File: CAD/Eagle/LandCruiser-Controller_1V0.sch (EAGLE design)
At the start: 37 parts, among them U101 MEGA8-P, U221 SN75240, U301 MIC2981/2982, U511 LM7805, X201 WEIDMUELLER 1234600000, X321 WEIDMUELLER 1234600000, X401 I2C

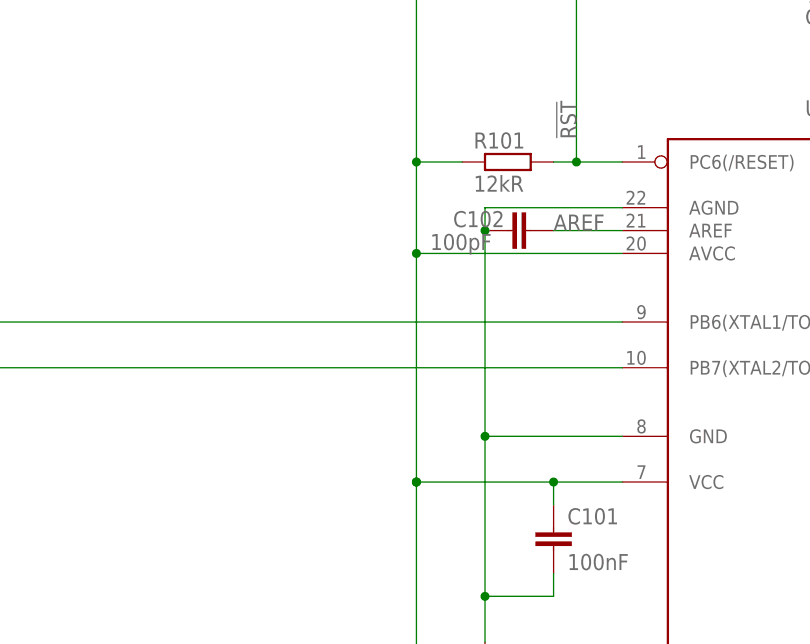
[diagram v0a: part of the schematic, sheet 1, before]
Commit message: HW_V1.0 - MPU - AVCC with 10uH for better ADC results
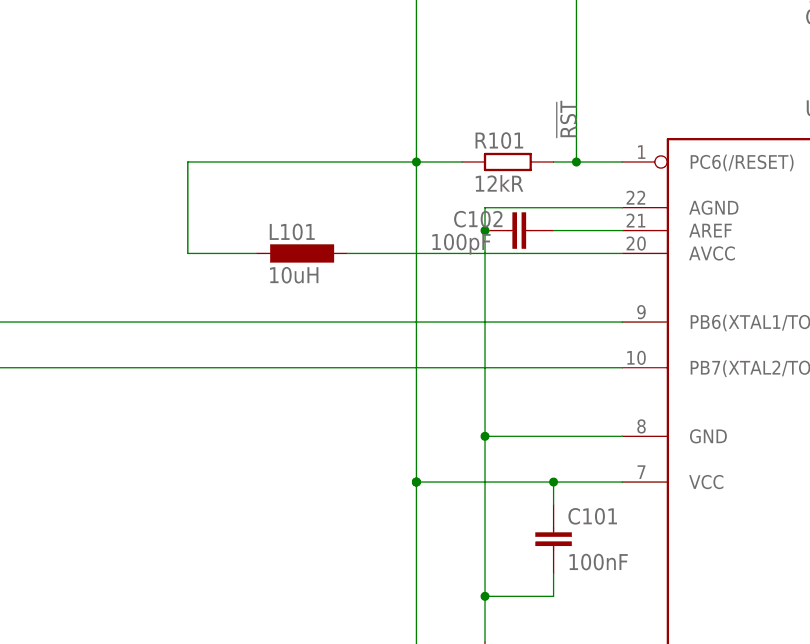
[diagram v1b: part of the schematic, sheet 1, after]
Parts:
- added L101: 10uH, rcl:L-EUL1812
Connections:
- net AREF renamed MP_AREF
- new net MP_AVCC: L101.1, U101.AVCC
- net +5V: now also L101.2; no longer U101.AVCC
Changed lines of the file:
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@@
 <part name="P+12V_1" library="df4iah_supply" deviceset="+12V" device=""/>
 <part name="FRAME7" library="df4iah_frame" deviceset="A4L-LOC" device="" value="I2C connector"/>
+<part name="L101" library="rcl" deviceset="L-EU" device="L1812" value="10uH"/>
 </parts>
 <sheets>
@@
 <instance part="X111" gate="G$1" x="124.46" y="152.4"/>
 <instance part="GND111" gate="1" x="134.62" y="137.16"/>
+<instance part="L101" gate="G$1" x="76.2" y="109.22" rot="R270"/>
 </instances>
 <busses>
@@
 </segment>
 </net>
-<net name="AREF" class="0">
+<net name="MP_AREF" class="0">
 <segment>
 <pinref part="C102" gate="G$1" pin="2"/>
 <wire x1="104.14" y1="111.76" x2="111.76" y2="111.76" width="0.1524" layer="91"/>
 <pinref part="U101" gate="G$1" pin="AREF"/>
-<label x="104.14" y="111.76" size="1.778" layer="95"/>
 </segment>
 </net>
@@
 <wire x1="88.9" y1="167.64" x2="88.9" y2="162.56" width="0.1524" layer="91"/>
 <wire x1="88.9" y1="162.56" x2="88.9" y2="119.38" width="0.1524" layer="91"/>
-<wire x1="88.9" y1="119.38" x2="88.9" y2="109.22" width="0.1524" layer="91"/>
-<wire x1="88.9" y1="109.22" x2="88.9" y2="83.82" width="0.1524" layer="91"/>
+<wire x1="88.9" y1="119.38" x2="88.9" y2="83.82" width="0.1524" layer="91"/>
 <junction x="88.9" y="83.82"/>
 <wire x1="88.9" y1="119.38" x2="93.98" y2="119.38" width="0.1524" layer="91"/>
 <junction x="88.9" y="119.38"/>
 <pinref part="R101" gate="G$1" pin="1"/>
-<pinref part="U101" gate="G$1" pin="AVCC"/>
-<wire x1="111.76" y1="109.22" x2="88.9" y2="109.22" width="0.1524" layer="91"/>
-<junction x="88.9" y="109.22"/>
 <pinref part="U101" gate="G$1" pin="VCC@1"/>
 <wire x1="88.9" y1="83.82" x2="104.14" y2="83.82" width="0.1524" layer="91"/>
@@
 <wire x1="104.14" y1="83.82" x2="104.14" y2="81.28" width="0.1524" layer="91"/>
 <junction x="104.14" y="83.82"/>
-</segment>
-</net>
+<wire x1="88.9" y1="119.38" x2="63.5" y2="119.38" width="0.1524" layer="91"/>
+<wire x1="63.5" y1="119.38" x2="63.5" y2="109.22" width="0.1524" layer="91"/>
+<pinref part="L101" gate="G$1" pin="2"/>
+<wire x1="63.5" y1="109.22" x2="71.12" y2="109.22" width="0.1524" layer="91"/>
+</segment>
+</net>
+<net name="MP_AVCC" class="0">
+<segment>
+<pinref part="U101" gate="G$1" pin="AVCC"/>
+<pinref part="L101" gate="G$1" pin="1"/>
+<wire x1="111.76" y1="109.22" x2="81.28" y2="109.22" width="0.1524" layer="91"/>
+</segment>
+</net>

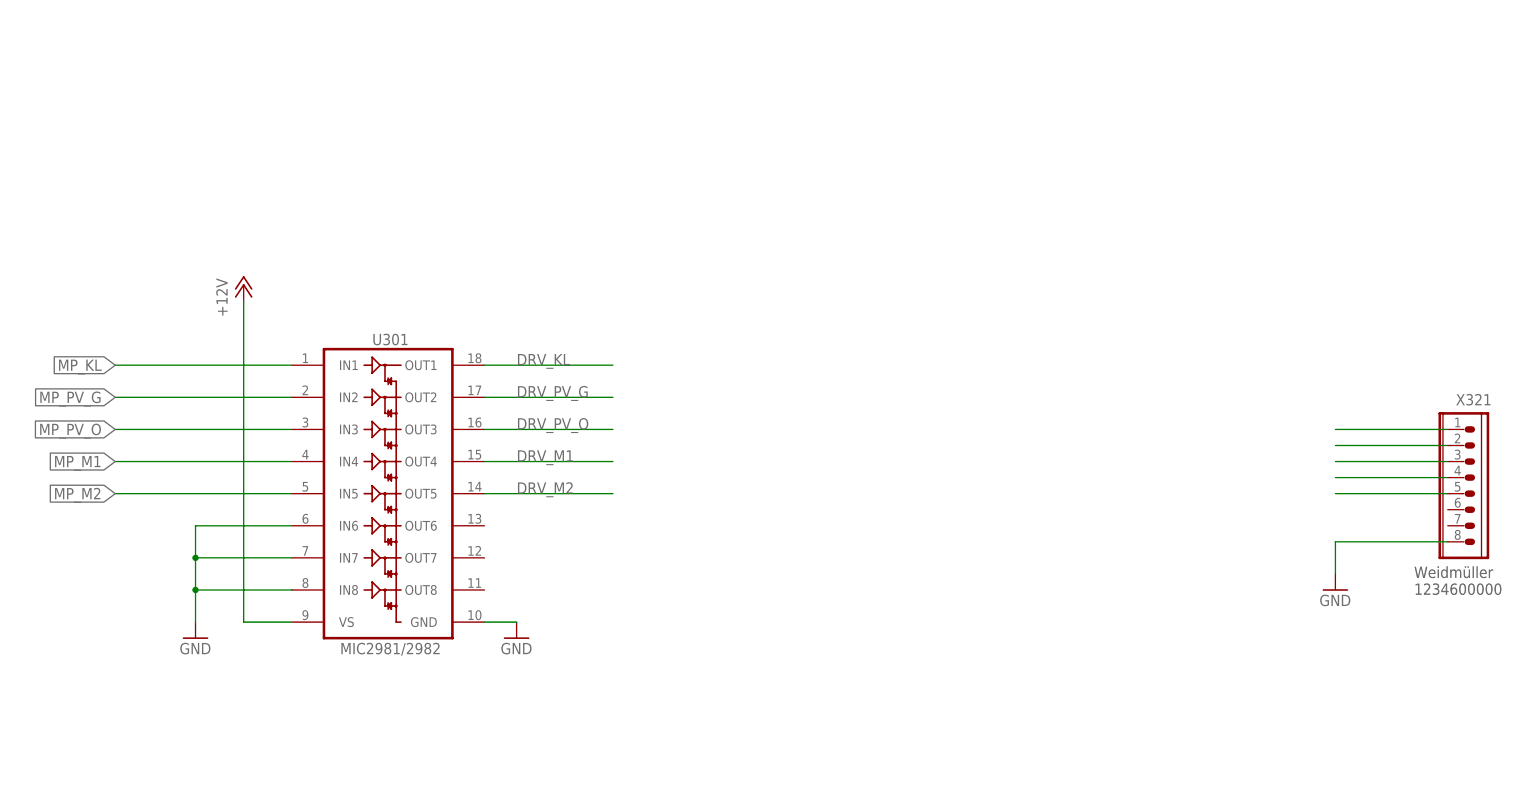
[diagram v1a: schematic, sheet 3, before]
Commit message: HW_V1.0 - OUTPUT - relay units added
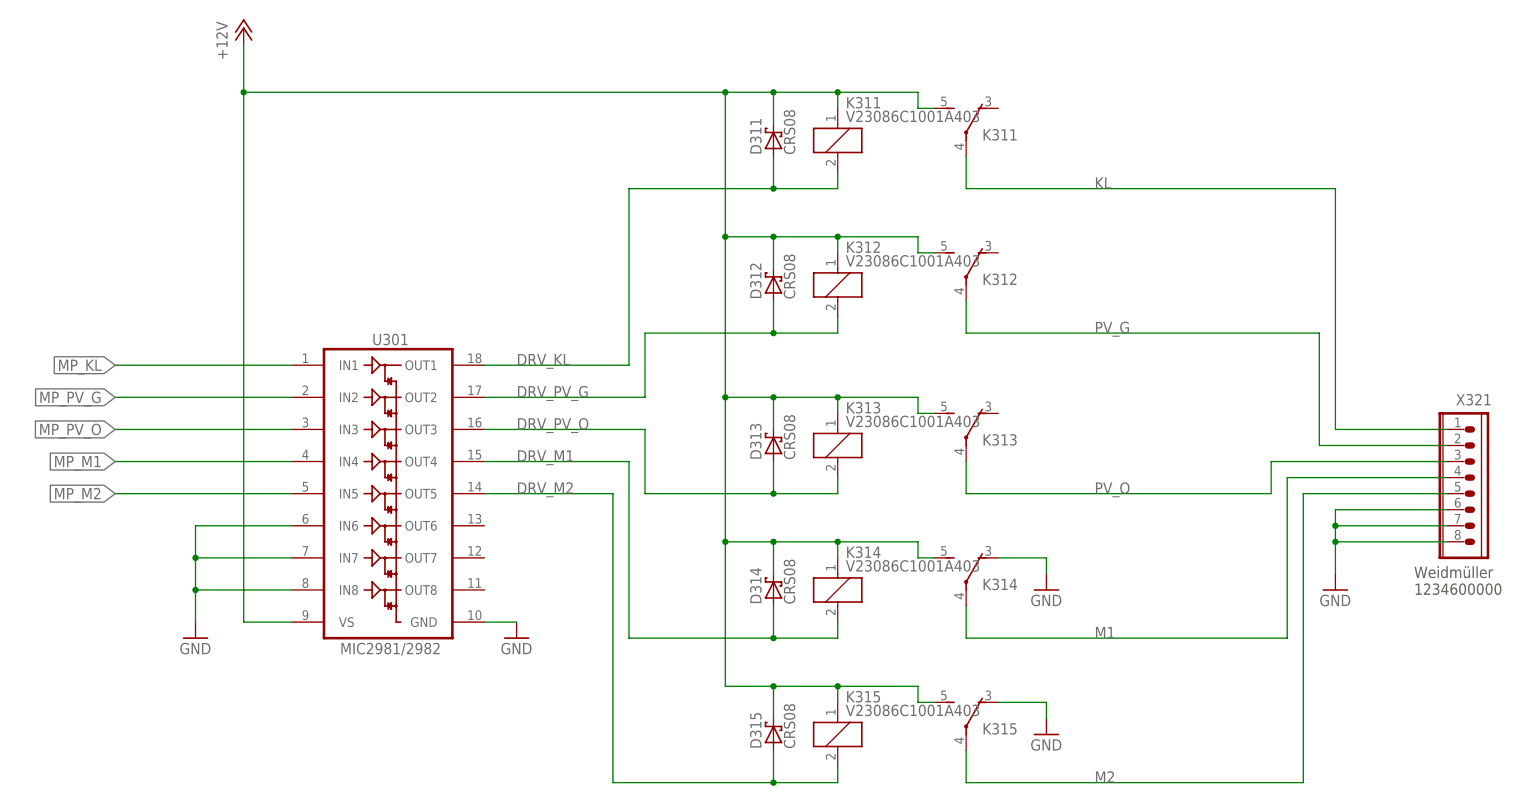
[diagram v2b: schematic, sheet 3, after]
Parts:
- added D311, D312, D313, D314, D315: CRS08, df4iah_diode:CRS08
- added K311, K312, K313, K314, K315: V23086C1001A403, df4iah_relay:V23086C1001A403
- F501: device fuse:SH22,5 -> df4iah_fuse:SH22,5
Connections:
- net +12V: now also D311.C, D312.C, D313.C, D314.C, D315.C, K3111.1, K3112.S, K3121.1, K3122.S, K3131.1, K3132.S, K3141.1, K3142.S, K3151.1, K3152.S
- net DRV_KL: now also D311.A, K3111.2
- net DRV_M1: now also D314.A, K3141.2
- net DRV_M2: now also D315.A, K3151.2
- net DRV_PV_G: now also D312.A, K3121.2
- net DRV_PV_O: now also D313.A, K3131.2
- net GND: now also K3142.O, K3152.O, X201.6, X321.6, X321.7
- net KL: now also K3112.P
- net M1: now also K3142.P
- net M2: now also K3152.P
- net PV_G: now also K3122.P
- net PV_O: now also K3132.P
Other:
- moved on the sheet: C102

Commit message: HW_V1.0 - V24 level shifter connected, Tacho input signal added
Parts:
- removed F501: 500 mA (S), df4iah_fuse:SH22,5
- removed H611, H612: MOUNT-HOLE1.7, df4iah_holes:MOUNT-HOLE1.7
- added C502, C503, C504, C511: 1uF, rcl:C-EUC0805
- added C601: 22uF, rcl:CPOL-EUE2.5-7
- added F601: 15 A (S), df4iah_fuse:FUSEMCCQ-121
- added F602: 500 mA (S), df4iah_fuse:FUSEMCCQ-121
- added IC501: MAX232, df4iah_dataconvertion:MAX232
- added R231: 10kR, rcl:R-EU_0309/12
- added R232: 22kR, rcl:R-EU_0309/12
- added X511: (no value), df4iah_connector:HEADER-2X2
- C401: device rcl:C-EU050-035X075 -> rcl:C-EUC0805
- C501: value 22uF -> 1uF; device rcl:CPOL-EUE2.5-7 -> rcl:C-EUC0805
- R491, R492: device rcl:R-EU_0309/12 -> rcl:R-EU_R0805
- renumbered C521 to C621, D501 to D601, H601 to H701, H602 to H702, H603 to H703, H604 to H704, U511 to U611
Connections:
- new net MP_TACHO: R231.2, R232.1, U101.PC2(ADC2)
- new net MX_C1N: C501.2, IC501G$1.C1-
- new net MX_C1P: C501.1, IC501G$1.C1+
- new net MX_C2M: C502.2, IC501G$1.C2-
- new net MX_C2P: C502.1, IC501G$1.C2+
- new net MX_VM: C504.1, IC501G$1.V-
- new net MX_VP: C503.1, IC501G$1.V+
- new net N$1: C601.+, D601.C, F602.2, U611.VI
- new net RXD: IC501G$1.R1IN, X511.2
- new net TACHO: R232.2, X201.1
- new net TXD: IC501G$1.T1OUT, X511.1
- net +12V: now also F601.2; no longer C501.+, D601.C, F501.2, U611.VI
- net +5V: now also C511.1, IC501P.VCC
- net +UB: now also F601.1, F602.1; no longer F501.1
- net ECU_FB: now also X201.2; no longer X201.1
- net GND: now also C503.2, C504.2, C511.2, C601.-, IC501G$1.R2IN, IC501G$1.T2IN, IC501P.GND, R231.1; no longer C501.-, X201.6
- net MP_RXD: now also IC501G$1.R1OUT
- net MP_TXD: now also IC501G$1.T1IN
- net SA_G: now also X201.5; no longer X201.4
- net SA_O: now also X201.6; no longer X201.5
- net SK_G: now also X201.3; no longer X201.2
- net SK_O: now also X201.4; no longer X201.3

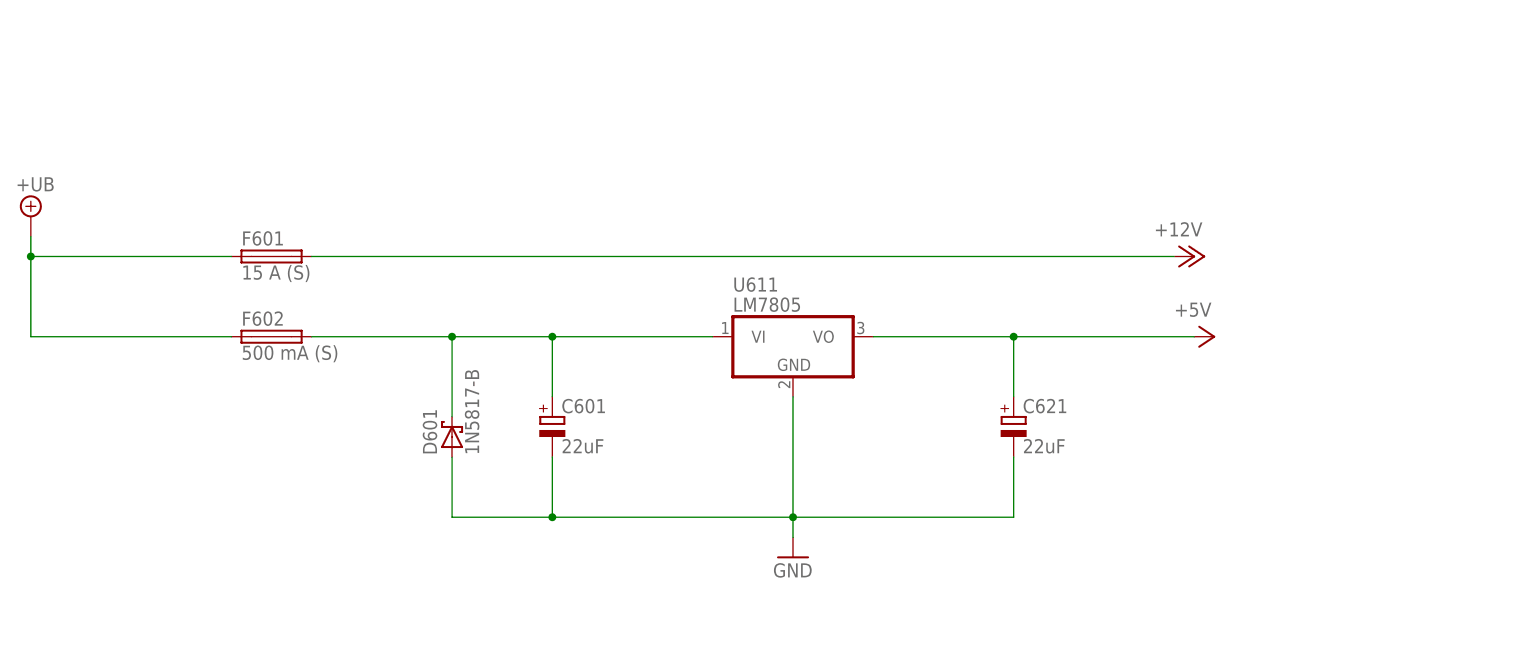
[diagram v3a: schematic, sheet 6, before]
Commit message: HW_V1.0 - changed most devices to SMD variants
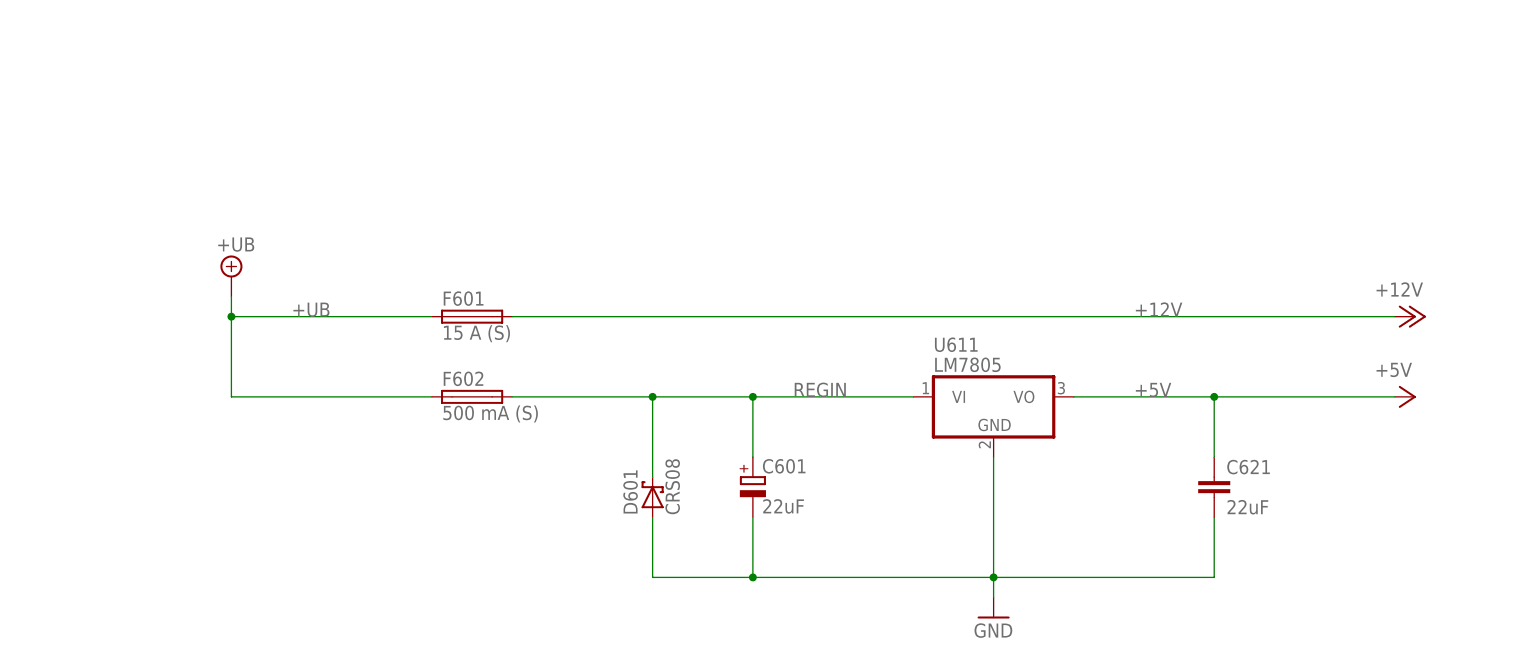
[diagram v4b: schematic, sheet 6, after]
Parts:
- removed IC501: MAX232, df4iah_dataconvertion:MAX232
- added U501: MAX232_SOIC16, df4iah_dataconvertion:MAX232_SOIC16
- C101, C102: device rcl:C-EU050-035X075 -> rcl:C-EUC0805
- C621: device rcl:CPOL-EUE2.5-7 -> rcl:C-EUC0805
- D601: value 1N5817-B -> CRS08; device df4iah_diode:1N5817-B -> df4iah_diode:CRS08
- F601, F602: device df4iah_fuse:FUSEMCCQ-121 -> df4iah_fuse:MCCQ-121
- R101, R121, R122, R123, R131, R132, R133, R134, R135, R211, R212, R213, R214, R215, R231, R232: device rcl:R-EU_0309/12 -> rcl:R-EU_R0805
- U301: value MIC2981/2982 -> MIC2981/2982SO18W; device df4iah_dataconvertion:MIC2981/2982 -> df4iah_dataconvertion:MIC2981/2982SO18W
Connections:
- net N$1 renamed REGIN
- net +5V: now also C621.1, U501P.VCC; no longer C621.+, IC501P.VCC
- net GND: now also C621.2, U501G$1.R2IN, U501G$1.T2IN, U501P.GND; no longer C621.-, IC501G$1.R2IN, IC501G$1.T2IN, IC501P.GND
- net MP_RXD: now also U501G$1.R1OUT; no longer IC501G$1.R1OUT
- net MP_TXD: now also U501G$1.T1IN; no longer IC501G$1.T1IN
- net MX_C1N: now also U501G$1.C1-; no longer IC501G$1.C1-
- net MX_C1P: now also U501G$1.C1+; no longer IC501G$1.C1+
- net MX_C2M: now also U501G$1.C2-; no longer IC501G$1.C2-
- net MX_C2P: now also U501G$1.C2+; no longer IC501G$1.C2+
- net MX_VM: now also U501G$1.V-; no longer IC501G$1.V-
- net MX_VP: now also U501G$1.V+; no longer IC501G$1.V+
- net RXD: now also U501G$1.R1IN; no longer IC501G$1.R1IN
- net TXD: now also U501G$1.T1OUT; no longer IC501G$1.T1OUT
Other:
- note added: "X511-1 = TXD X511-2 = RXD X511-3 = N.C. X511-4 = N.C."
- moved on the sheet: C601, D601, F601, F602, U611

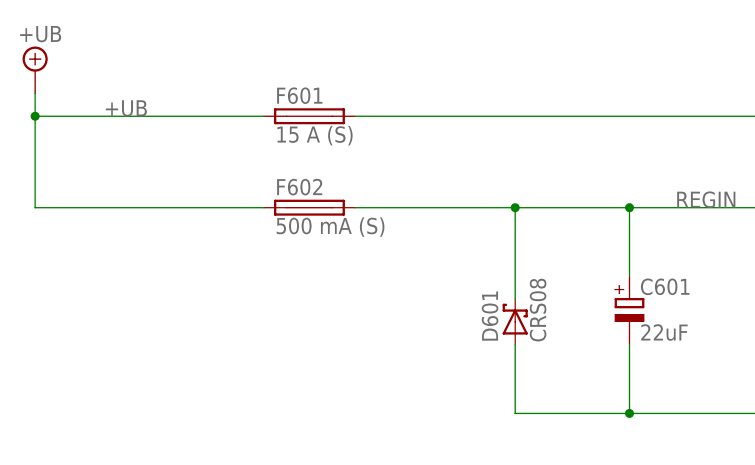
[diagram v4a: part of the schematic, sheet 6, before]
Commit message: HW_V1.0 - df4iah_fuse.lbr - trying to fix the restring issue
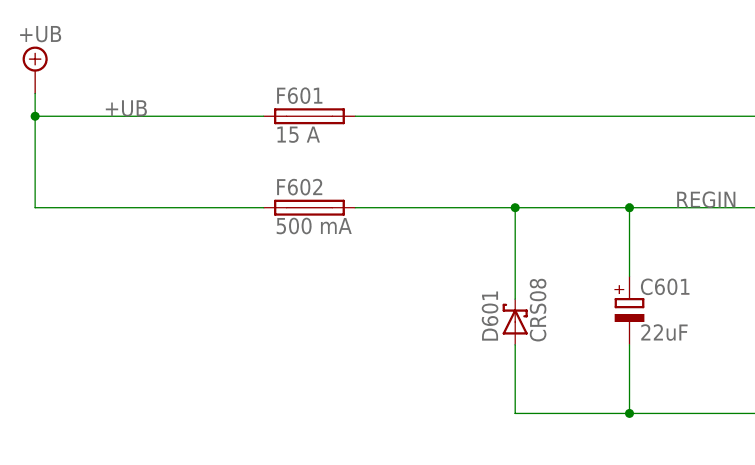
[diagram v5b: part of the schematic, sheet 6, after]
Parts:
- F601: value 15 A (S) -> 15 A
- F602: value 500 mA (S) -> 500 mA
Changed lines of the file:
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@@
 <part name="SUPPLY1" library="df4iah_supply" deviceset="+UB" device=""/>
 <part name="SUPPLY_601" library="df4iah_supply" deviceset="+UB" device=""/>
-<part name="F602" library="df4iah_fuse" deviceset="MCCQ-121" device="" value="500 mA (S)"/>
 <part name="X321" library="df4iah_connector" deviceset="WIRE-TO-BOARD_5MM08_1X08" device="" value="WEIDMUELLER 1234600000"/>
 <part name="GND321" library="df4iah_supply" deviceset="GND" device=""/>
@@
 <part name="C501" library="rcl" deviceset="C-EU" device="C0805" value="1uF"/>
 <part name="C502" library="rcl" deviceset="C-EU" device="C0805" value="1uF"/>
-<part name="F601" library="df4iah_fuse" deviceset="MCCQ-121" device="" value="15 A (S)"/>
 <part name="C503" library="rcl" deviceset="C-EU" device="C0805" value="1uF"/>
 <part name="C504" library="rcl" deviceset="C-EU" device="C0805" value="1uF"/>
@@
 <part name="R231" library="rcl" deviceset="R-EU_" device="R0805" value="10kR"/>
 <part name="GND2" library="df4iah_supply" deviceset="GND" device=""/>
+<part name="F601" library="df4iah_fuse" deviceset="MCCQ-121" device="" value="15 A"/>
+<part name="F602" library="df4iah_fuse" deviceset="MCCQ-121" device="" value="500 mA"/>
 </parts>
 <sheets>
@@
 <instance part="C601" gate="G$1" x="119.38" y="86.36"/>
 <instance part="SUPPLY_601" gate="G$1" x="53.34" y="111.76"/>
-<instance part="F602" gate="G$1" x="83.82" y="96.52"/>
 <instance part="D601" gate="G$1" x="106.68" y="83.82" rot="R90"/>
 <instance part="F601" gate="G$1" x="83.82" y="106.68"/>
+<instance part="F602" gate="G$1" x="83.82" y="96.52"/>
 </instances>
 <busses>
@@
 <pinref part="P+12V_601" gate="1" pin="+12V"/>
 <wire x1="200.66" y1="106.68" x2="88.9" y2="106.68" width="0.1524" layer="91"/>
+<label x="167.64" y="106.68" size="1.778" layer="95"/>
 <pinref part="F601" gate="G$1" pin="2"/>
-<label x="167.64" y="106.68" size="1.778" layer="95"/>
 </segment>
 </net>
@@
 <wire x1="53.34" y1="106.68" x2="53.34" y2="96.52" width="0.1524" layer="91"/>
 <wire x1="53.34" y1="96.52" x2="78.74" y2="96.52" width="0.1524" layer="91"/>
-<pinref part="F602" gate="G$1" pin="1"/>
-<pinref part="F601" gate="G$1" pin="1"/>
 <junction x="53.34" y="106.68"/>
 <label x="60.96" y="106.68" size="1.778" layer="95"/>
 <wire x1="78.74" y1="106.68" x2="53.34" y2="106.68" width="0.1524" layer="91"/>
+<pinref part="F601" gate="G$1" pin="1"/>
+<pinref part="F602" gate="G$1" pin="1"/>
 </segment>
 </net>
@@
 <junction x="106.68" y="96.52"/>
 <wire x1="88.9" y1="96.52" x2="106.68" y2="96.52" width="0.1524" layer="91"/>
+<label x="124.46" y="96.52" size="1.778" layer="95"/>
 <pinref part="F602" gate="G$1" pin="2"/>
-<label x="124.46" y="96.52" size="1.778" layer="95"/>
-</segment>
-</net>
+</segment>
+</net>
